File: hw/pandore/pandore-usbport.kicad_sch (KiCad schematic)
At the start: 35 parts, among them J2 USB2-A_2stacked, J3 USB3-A_2stacked, U29 5.5V 1A, U30 5.5V 1A, U31 5.5V 1A, U32 5.5V 1A

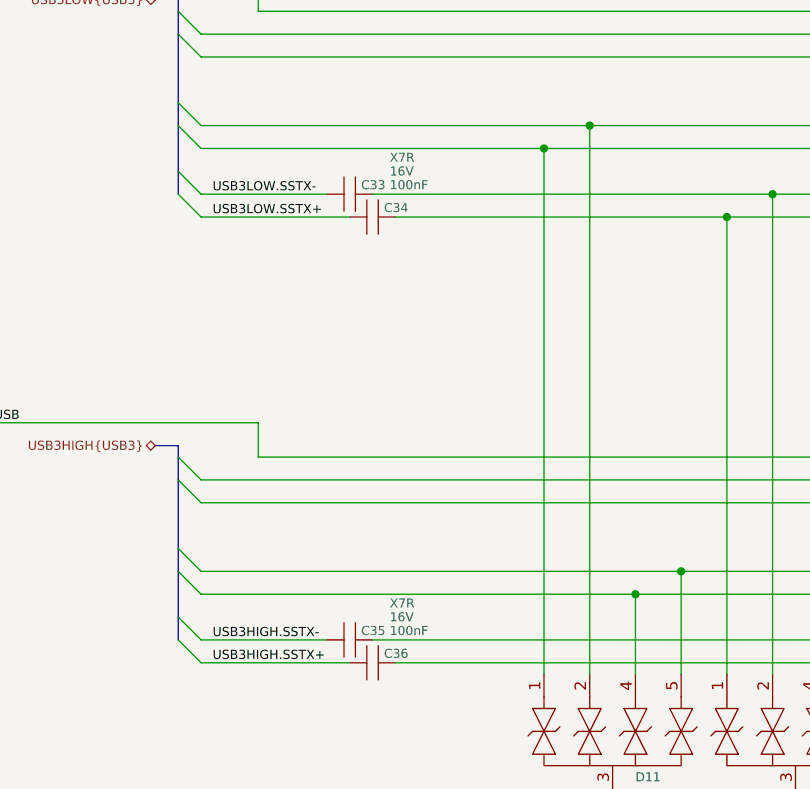
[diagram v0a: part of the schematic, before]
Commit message: finished adding mpn,mfg to all parts, finished routing placement
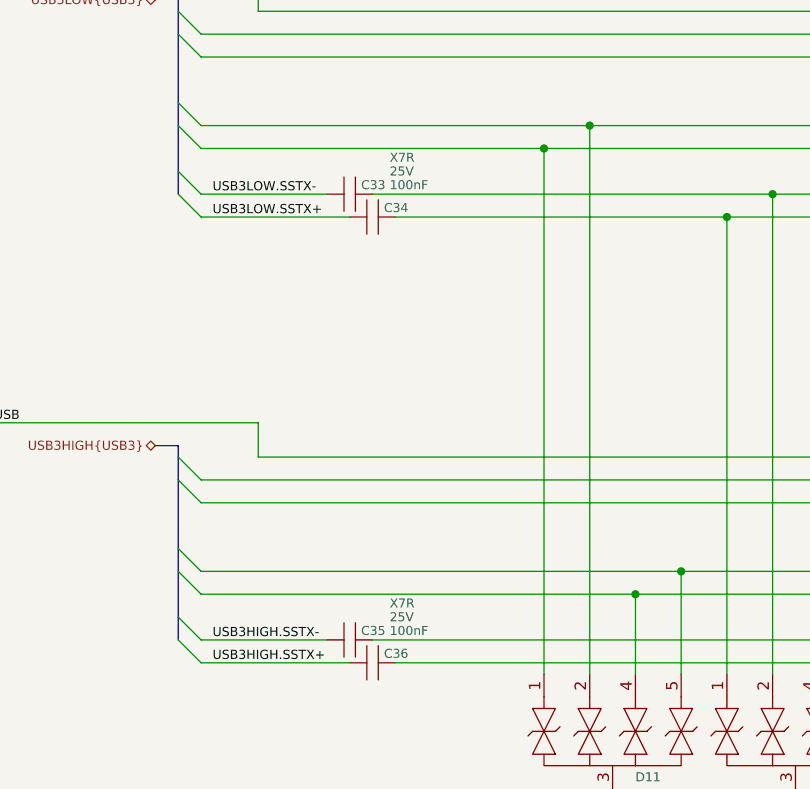
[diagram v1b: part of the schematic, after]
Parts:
- C265, C266, C267, C268, C269, C270, C271, C272: MFG (none) -> KEMET; MPN (none) -> C0603C105K4RACTU
- C274, C275, C276, C277: MFG (none) -> Murata; MPN (none) -> GRM21BR61E106KA73K
- C33, C34, C35, C36: MFG2 Samsung Electro-Mechanics -> (none); MFG3 Taiyo Yuden -> (none); MPN2 CL05B104KA5NNNC -> (none); MPN3 EMK105B7104KV-F -> (none); Voltage 16V -> 25V
- R48, R49: Link (none) -> https://yageogroup.com/products/Resistors/part/RC0402JR-070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; MFG (none) -> Yageo; MFG2 (none) -> Stackpole; MFG3 (none) -> Vishay Dale; MPN (none) -> RC0402JR-070RL; MPN2 (none) -> RMCF0402ZT0R00; MPN3 (none) -> CRCW04020000Z0ED
